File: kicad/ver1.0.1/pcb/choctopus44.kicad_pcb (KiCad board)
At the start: 2 copper layers, 243.9 x 111.9 mm, 110 parts, among them SW1 SW_PUSH, SW10 SW_PUSH, SW11 SW_PUSH, SW12 SW_PUSH, SW13 SW_PUSH, SW14 SW_PUSH, SW15 SW_PUSH, SW16 SW_PUSH, SW17 SW_PUSH, SW18 SW_PUSH, SW19 SW_PUSH, SW2 SW_PUSH, SW20 SW_PUSH, SW21 SW_PUSH, SW22 SW_PUSH, SW23 SW_PUSH, SW24 SW_PUSH, SW25 SW_PUSH, SW26 SW_PUSH, SW27 SW_PUSH, SW28 SW_PUSH, SW29 SW_PUSH, SW3 SW_PUSH, SW30 SW_PUSH, SW31 SW_PUSH, SW32 SW_PUSH, SW33 SW_PUSH, SW34 SW_PUSH, SW35 SW_PUSH, SW36 SW_PUSH, SW37 SW_PUSH, SW38 SW_PUSH, SW39 SW_PUSH, SW4 SW_PUSH, SW40 SW_PUSH, SW41 SW_PUSH, SW42 SW_PUSH, SW43 SW_PUSH, SW44 SW_PUSH, SW45 Rotary_Encoder_Switch, SW5 SW_PUSH, SW6 SW_PUSH, SW7 SW_PUSH, SW8 SW_PUSH, SW9 SW_PUSH, U1 ProMicro

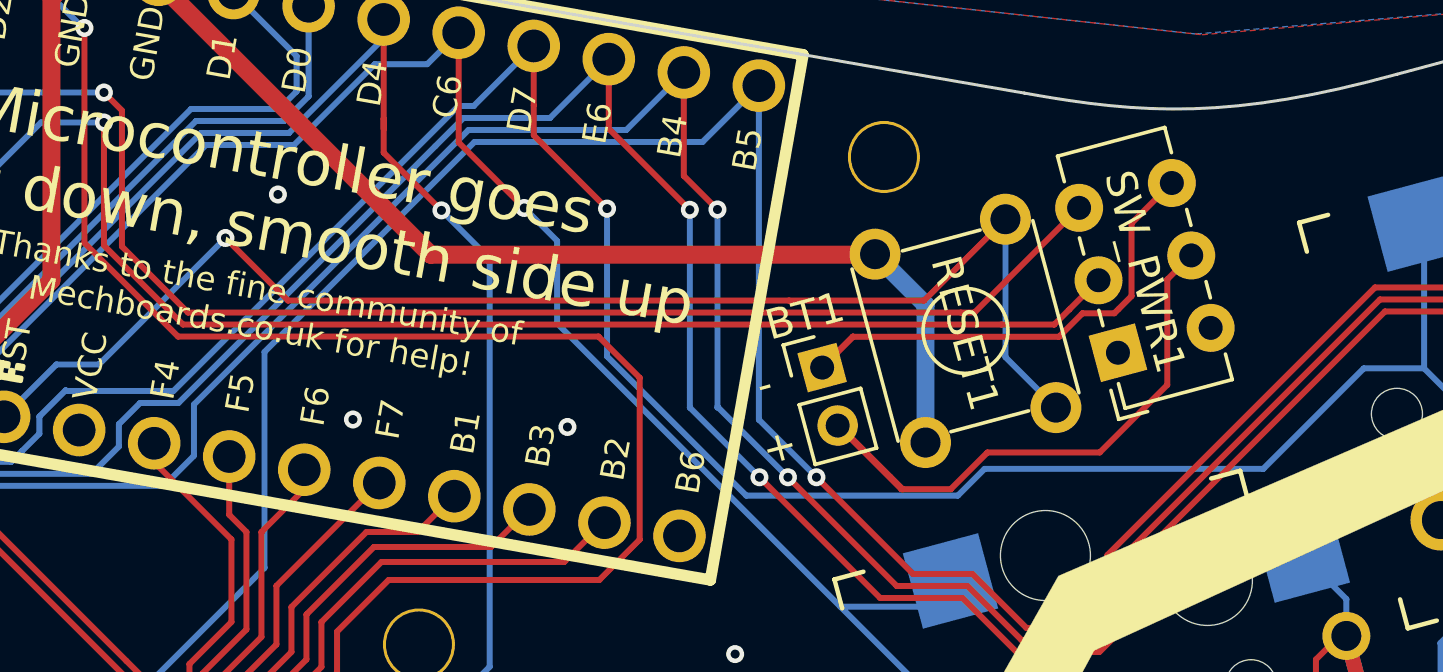
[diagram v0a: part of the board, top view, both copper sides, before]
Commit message: sorted PCB *and schematic some more*
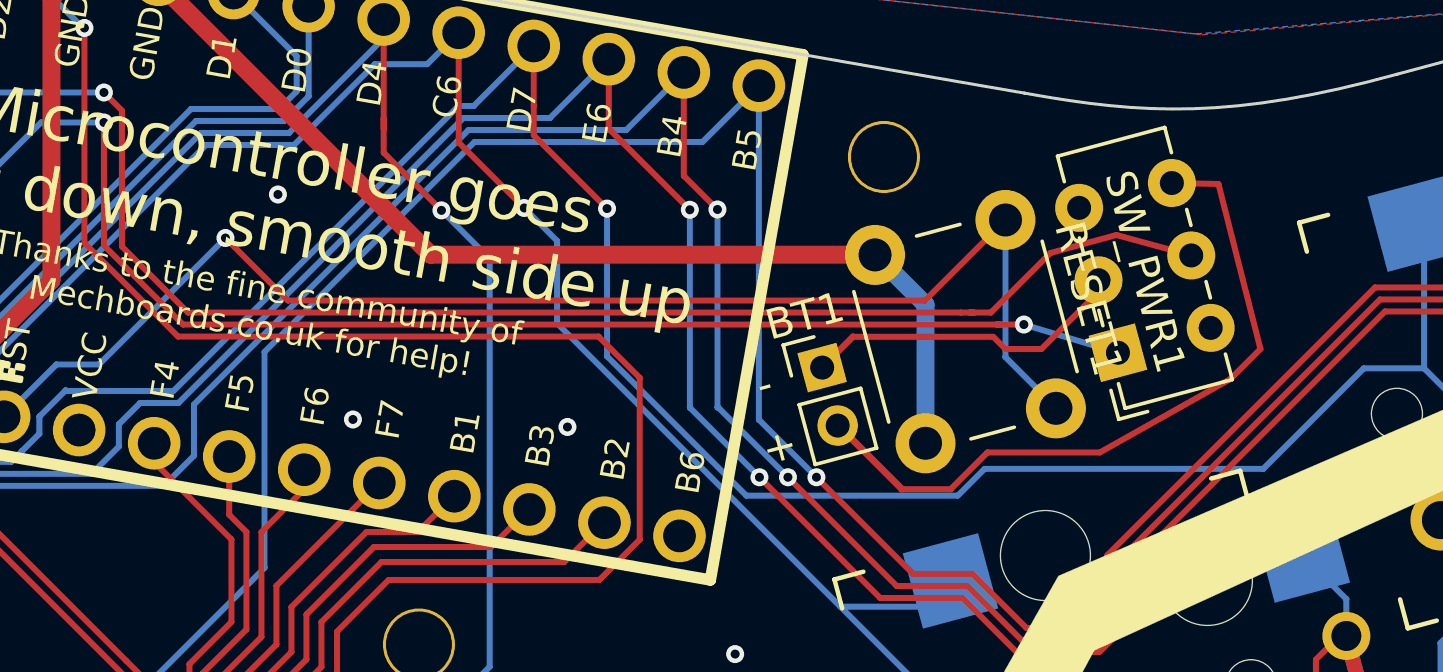
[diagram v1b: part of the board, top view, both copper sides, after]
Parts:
- RESET1: value SW_PUSH -> SW_Push; footprint Button_Switch_THT:SW_TH_Tactile_Omron_B3F-10xx -> Button_Switch_THT:SW_PUSH_6mm
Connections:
- RESET1 pad 2: reset -> GND
- SW_PWR1 pad 1: +BATT -> Net-(BT1-Pad1)
- SW_PWR1 pad 2: Net-(BT1-Pad2) -> -BATT
- SW_PWR1 pad 3: -BATT -> Net-(SW_PWR1-Pad3)
- SW_PWR1 pad 4: Net-(BT1-Pad1) -> Net-(BT1-Pad2)
- SW_PWR1 pad 5: (no net) -> +BATT
- SW_PWR1 pad 6: (no net) -> Net-(SW_PWR1-Pad6)
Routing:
- net Net-(BT1-Pad2): track 21.0 -> 26.8 mm
- net Net-(BT1-Pad1): track 17.1 -> 12.4 mm
- net -BATT: track 52.7 -> 56.1 mm
- net +BATT: track 53.3 -> 53.6 mm, vias 1 -> 2
